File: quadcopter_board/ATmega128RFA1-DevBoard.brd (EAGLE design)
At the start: 57.1 x 53.3 mm, 44 parts, among them J1 ISP, J2 ARDUINO_UNO_R3, J3 POWER_JACKPTH_LOCK, U1 ATMEGA128RFA1, U2 LM1117, Y1 16MHz

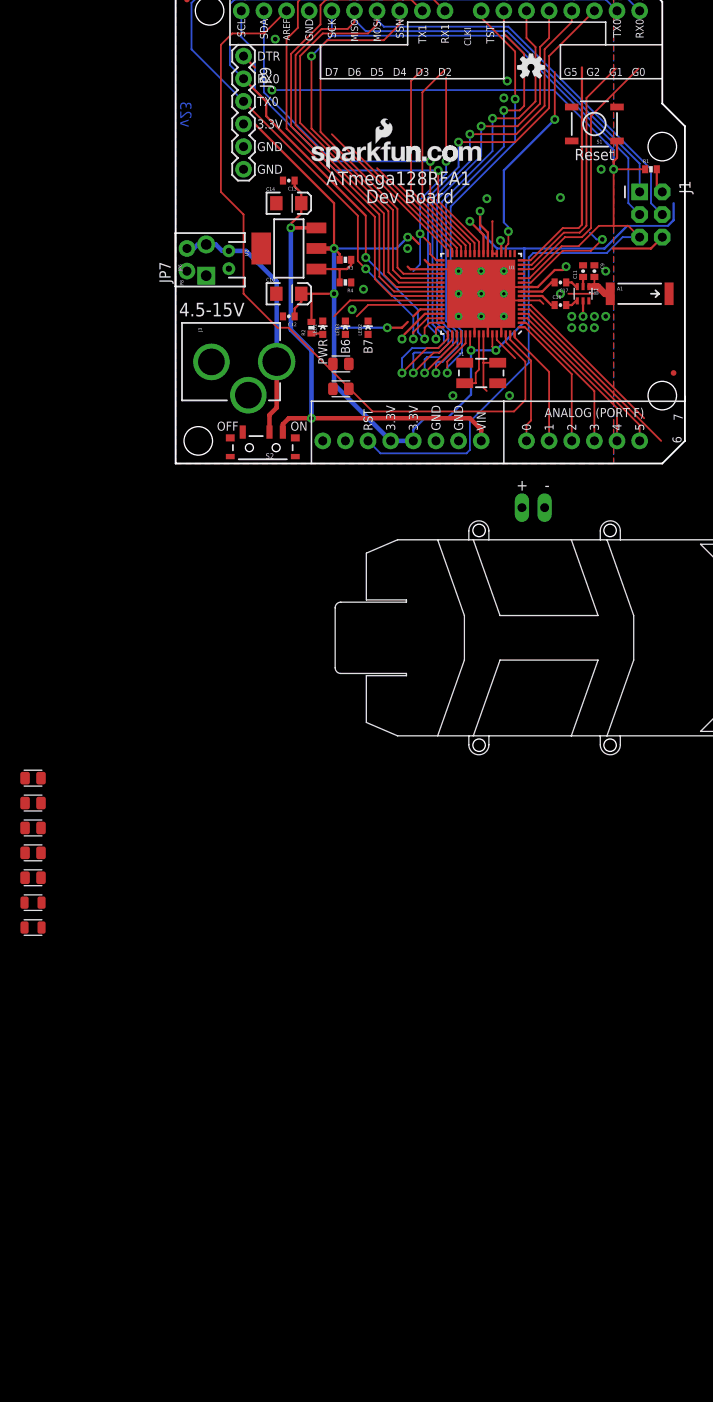
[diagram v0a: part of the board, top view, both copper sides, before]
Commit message: added and wired imu
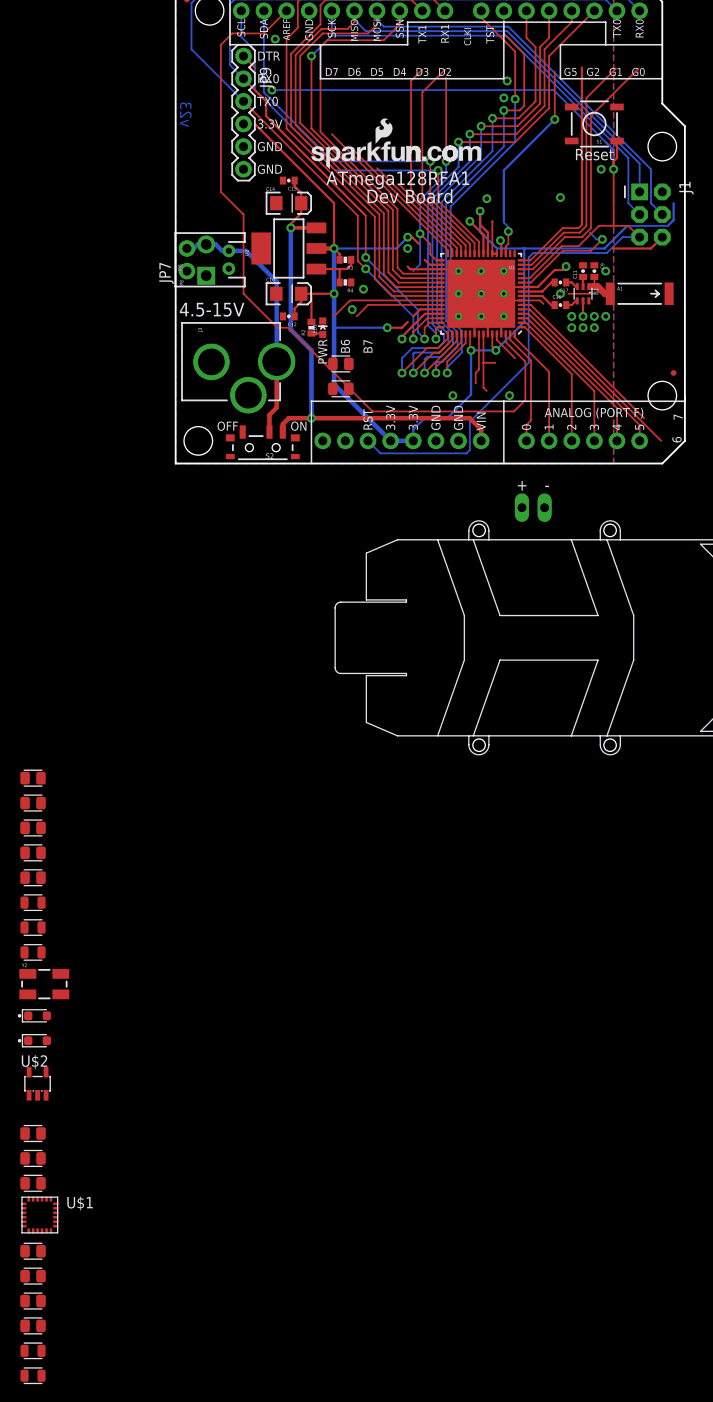
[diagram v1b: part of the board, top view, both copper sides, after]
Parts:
- removed LED2, LED3: GREEN, SparkFun-LED:LED-0603
- removed Y1: 16MHz, SparkFun-FreqCtrl:CRYSTAL-SMD-5X3
- added C1, C2: 1uF, quadparts_prebuilt:CAPC2012X140_HS
- added C18: 0.01uF, quadparts_prebuilt:CAPC2012X140_HS
- added C19: 0.1uF, quadparts_prebuilt:CAPC2012X140_HS
- added C20: 10uF, quadparts_prebuilt:CAPC2012X140_HS
- added C21: 4.7uF, quadparts_prebuilt:CAPC2012X140_HS
- added C22: 0.22uF, quadparts_prebuilt:CAPC2012X140_HS
- added D1, D2: green, quadparts_prebuilt:LEDSC125X200X120-2_HS
- added R5, R6: 10K, quadparts_prebuilt:RESC2012X60_HS
- added U$2: TPS73633-DBVT, quadparts_prebuilt:SOT23-DBV
- added Y2: (no value), quadparts_prebuilt:CRYSTAL-SMD-5X3
- R1: value 10k -> 10K; device SparkFun-Passives:0402-RES -> quadparts_prebuilt:RESC2012X60_HS
- U$1: value OSHW-LOGOS -> IMU; device SparkFun-Aesthetics:OSHW-LOGO-S -> quadparts:LGA-24_4X4MM
- moved R1 149.6 mm to (-16.0, -99.6)
- moved U$1 140.1 mm to (-15.2, -84.3)
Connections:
- new net BAT_GND: BATT1.-, C1.2, C18.2, C19.2, C2.2, C20.2, C21.1, U$1.P$2, U$1.P$22, U$1.P$23, U$1.P$3, U$1.P$4, U$1.P$5, U$1.P$6, U$2.2
- new net N$1: BATT1.+, C1.1, U$2.1, U$2.3
- new net N$12: C22.1, U$1.P$8
- new net N$14: C22.2, U$1.P$9
- new net N$15: R1.2, U$1.P$19
- new net N$16: R6.2, U$1.P$20
- new net N$5: C18.1, U$2.4
- new net N$6: C21.2, U$1.P$7
- net 3.3V: now also R5.2; no longer R1.2
- net GND: now also D1.C, D2.C; no longer LED2.C, LED3.C
- net N$13: now also D1.A; no longer LED2.A
- net N$3: now also Y2.3; no longer Y1.3
- net N$4: now also Y2.1; no longer Y1.1
- net N$8: now also D2.A; no longer LED3.A
- net RESET: now also R5.1; no longer R1.1
- net SCL: now also U$1.P$21
- net SDA: now also U$1.P$24
- net VCC: now also C19.1, C2.1, C20.1, R1.1, R6.1, U$1.P$15, U$1.P$16, U$1.P$17, U$1.P$18, U$2.5
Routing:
- net RESET: track 122.6 -> 119.1 mm
- net 3.3V: track 150.9 -> 149.0 mm
- net N$4: track 6.92 -> 5.70 mm

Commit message: added motor controller
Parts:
- removed J3: POWER_JACKPTH_LOCK, SparkFun-Connectors:POWER_JACK_PTH_LOCK
- removed JP6: (no value), SparkFun-Connectors:JST-2-PTH
- removed JP7: (no value), SparkFun-Connectors:1X02_NO_SILK
- removed JP8: (no value), SparkFun-Connectors:SCREWTERMINAL-3.5MM-2-NS
- added C23, C26, C29, C32: 1uf, Seeed-Capacitor-2016:C0402
- added C24, C27, C30, C33: 100uf, Seeed-Capacitor-2016:AVX-B
- added C25, C28, C31, C34: 1uf, Seeed-Capacitor-2016:C0603
- added D3, D4, D5, D6: 28V-5A, Seeed-Diode-2016:DO-214AA
- added J4: (no value), quadparts:MALE_HEADER_2X1_0.1IN
- added JP1: FTDI (Serial Only), SparkFun-Connectors:FTDI_BASIC
- added Q1, Q2, Q3, Q4: CJ2302, Seeed-Transistor-2016:SOT-23
- added R10, R12, R14, R16: 10K 1/10W, Seeed-Resistor-2016:R0603
- added R11, R13, R15, R9: 100R, Seeed-Resistor-2016:R0603
- added U$3: 0, quadparts:SMD_RESISTOR
- added U$4, U$5, U$6, U$7: MOTOR_PADS, Andranik-Lab4:MOTOR_PADS
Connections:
- removed net N$1: BATT1.+, C1.1, U$2.1, U$2.3
- new net N$17: BATT1.+, J4.1
- new net N$18: Q1.1, R10.2, R9.2
- new net N$19: C25.1, D3.+, Q1.3, U$4.V-
- new net N$21: Q2.1, R11.2, R12.2
- new net N$22: C28.1, D4.+, Q2.3, U$5.V-
- new net N$24: Q3.1, R13.2, R14.2
- new net N$25: C31.1, D5.+, Q3.3, U$6.V-
- new net N$27: Q4.1, R15.2, R16.2
- new net N$28: C34.1, D6.+, Q4.3, U$7.V-
- net 3.3V: now also C19.1, C2.1, C20.1, R1.1, R6.1, U$1.P$15, U$1.P$16, U$1.P$17, U$1.P$18, U$2.5
- net BAT_GND: now also C23.1, C24.-, C26.1, C27.-, C29.1, C30.-, C32.1, C33.-, Q1.2, Q2.2, Q3.2, Q4.2, R10.1, R12.1, R14.1, R16.1, U$3.P$1; no longer C1.2, C18.2, C19.2, C2.2, C20.2, C21.1, U$1.P$2, U$1.P$22, U$1.P$23, U$1.P$3, U$1.P$4, U$1.P$5, U$1.P$6, U$2.2
- net GND: now also C1.2, C18.2, C19.2, C2.2, C20.2, C21.1, JP1.GND, U$1.P$2, U$1.P$22, U$1.P$23, U$1.P$3, U$1.P$4, U$1.P$5, U$1.P$6, U$2.2, U$3.P$2; no longer J3.GND, J3.GNDBREAK, JP6.1, JP7.1, JP8.1
- net N$9: no longer J3.PWR, JP6.2, JP7.2, JP8.2
- net PB5: now also R9.1
- net PE3: now also R13.1
- net PE4: now also R15.1
- net PE5: now also R11.1
- net RX1: now also JP1.RXI
- net TX1: now also JP1.TXO
- net VCC: now also C1.1, C24.+, C25.2, C27.+, C28.2, C30.+, C31.2, C33.+, C34.2, D3.-, D4.-, D5.-, D6.-, J4.2, U$2.1, U$2.3, U$4.V+, U$5.V+, U$6.V+, U$7.V+; no longer C19.1, C2.1, C20.1, R1.1, R6.1, U$1.P$15, U$1.P$16, U$1.P$17, U$1.P$18, U$2.5
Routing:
- net N$9: track 29.2 -> 3.06 mm

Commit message: added bigger cap to power supply
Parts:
- removed C10, C14: 10uF, SparkFun-Passives:EIA3216
- removed LED1: RED, SparkFun-LED:LED-0603
- removed R2: 1k, SparkFun-Passives:0402-RES
- removed R3: 240, SparkFun:0402-RES
- removed R4: 390, SparkFun:0402-RES
- removed S2: (no value), SparkFun:SWITCH-SPST-SMD-A
- removed U2: LM1117, SparkFun:SOT223
- added C35: 220uF, quadparts_prebuilt:CAPMP7343X310_HS
- C1, C2: value 1uF -> 10uF
- moved C1 148.3 mm to (-16.0, -223.5)
- moved C2 148.3 mm to (-16.0, -226.3)
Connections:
- removed net FB: R3.1, R4.2, U2.1
- removed net N$2: LED1.A, R2.1
- removed net N$9: S2.2
- net 3.3V: no longer C10.A, R2.2, R3.2, U2.2
- net GND: no longer C10.C, C14.C, LED1.C, R4.1
- net VCC: no longer C14.A, S2.1, U2.3
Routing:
- net 3.3V: track 149.0 -> 141.1 mm
- net FB: track 6.15 -> 0.00 mm
- net VCC: track 56.5 -> 50.5 mm
- net N$9: track 3.06 -> 0.00 mm
- net N$2: track 1.31 -> 0.00 mm

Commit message: added tags
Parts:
- removed C12: 1uF, SparkFun-Passives:0402-CAP
- removed C13: 0.1uF, SparkFun-Passives:0402-CAP
- removed C35: 220uF, quadparts_prebuilt:CAPMP7343X310_HS
- removed J2: ARDUINO_UNO_R3, SparkFun-Boards:ARDUINO_UNO_R3
- removed S1: (no value), SparkFun-Electromechanical:TACTILE_SWITCH_SMD
- added C10: 0.75pF, quadparts_prebuilt:CAPC2012X140_HS
- added C14: 22pF, quadparts_prebuilt:CAPC2012X140_HS
- C16: value JUMP -> 1uF; device SparkFun:0402-CAP -> quadparts_prebuilt:CAPC2012X140_HS
- C17: value JUMP -> 0.1uF; device SparkFun:0402-CAP -> quadparts_prebuilt:CAPC2012X140_HS
- moved C17 264.5 mm to (-16.0, -237.5), turned to 0 degrees
- moved C16 259.3 mm to (-16.0, -234.7)
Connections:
- removed net N$10: B1.4, C16.2
- removed net N$11: B1.3, C17.1
- net 3.3V: now also C16.1; no longer C12.1, J2.3.3V, J2.5V
- net A0: no longer J2.A0
- net A1: no longer J2.A1
- net A2: no longer J2.A2
- net A3: no longer J2.A3
- net A4: no longer J2.A4
- net A5: no longer J2.A5
- net AREF: no longer J2.AREF
- net GND: now also C16.2, C17.2; no longer C12.2, C13.2, J2.GND@0, J2.GND@1, J2.GND@2, S1.3
- net MISO: no longer J2.D12
- net MOSI: no longer J2.D11
- net PB4: no longer J2.D9
- net PB5: no longer J2.D8
- net PE2: no longer J2.D2
- net PE3: no longer J2.D3
- net PE4: now also C32.2; no longer J2.D4
- net PE5: no longer J2.D5
- net PE6: no longer J2.D6
- net PE7: no longer J2.D7
- net RESET: no longer J2.RES, S1.1
- net RFN: now also B1.3; no longer C17.2
- net RFP: now also B1.4; no longer C16.1
- net RX0: no longer J2.RX
- net SCK: no longer J2.D13
- net SCL: no longer J2.SCL
- net SDA: no longer J2.SDA
- net SSN: no longer J2.D10
- net TX0: no longer J2.TX
- net VCC: now also C17.1; no longer C13.1, J2.VIN
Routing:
- net 3.3V: track 141.1 -> 71.2 mm, vias 7 -> 3
- net VCC: track 50.5 -> 0.00 mm, vias 2 -> 0
- net SDA: track 43.4 -> 34.3 mm
- net A1: track 13.6 -> 5.87 mm
- net A2: track 15.3 -> 7.84 mm
- net PE2: track 50.5 -> 43.3 mm
- net A3: track 17.0 -> 11.4 mm
- net RESET: track 119.1 -> 115.2 mm
- net A4: track 18.6 -> 14.9 mm
- net AREF: track 83.9 -> 80.3 mm
- net PE4: track 58.6 -> 55.5 mm
- net PE5: track 55.8 -> 52.7 mm
- net SCL: track 45.1 -> 42.1 mm
- net RX0: track 104.2 -> 101.3 mm
- net SCK: track 85.4 -> 82.6 mm
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
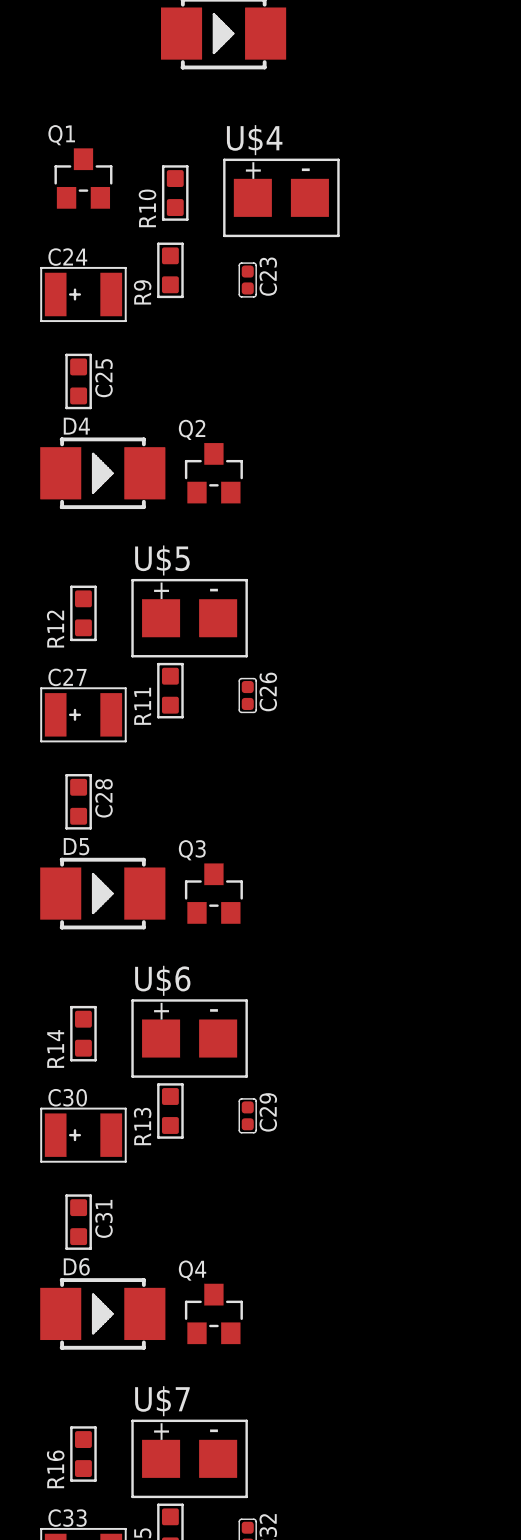
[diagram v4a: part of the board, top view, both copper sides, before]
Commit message: clear up of motor driver layout
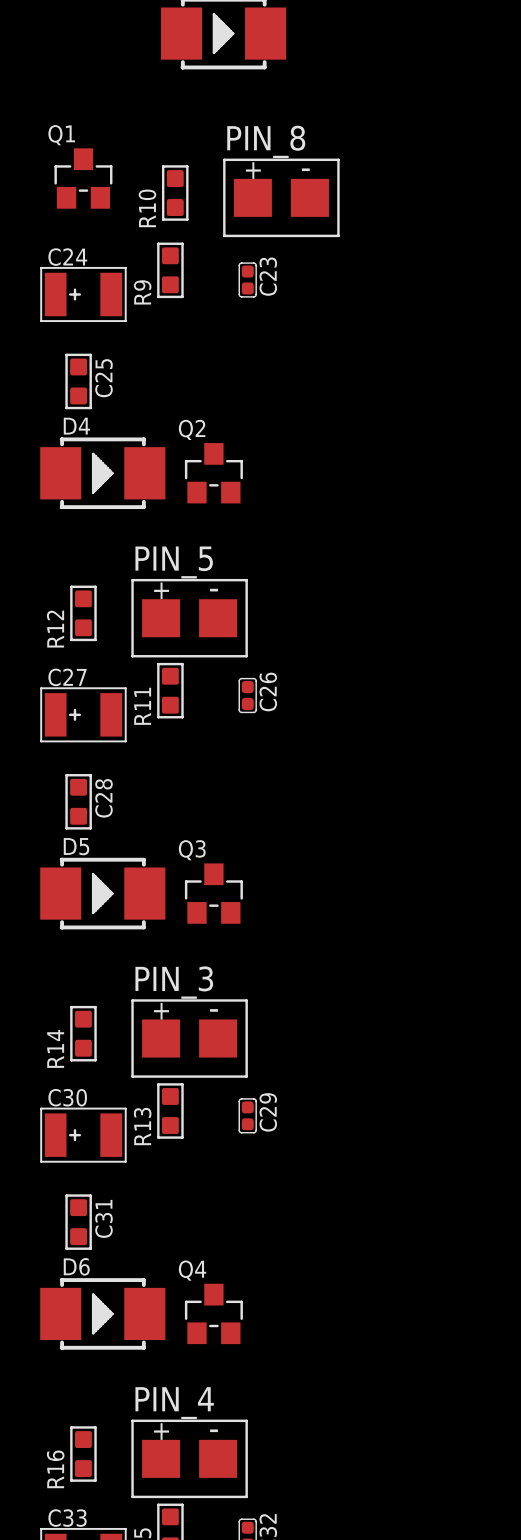
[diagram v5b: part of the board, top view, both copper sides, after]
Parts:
- renumbered U$4 to PIN_8, U$5 to PIN_5, U$6 to PIN_3, U$7 to PIN_4
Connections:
- net PB5: now also C23.2
- net PE3: now also C29.2
- net PE5: now also C26.2
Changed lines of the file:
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@@
 <attribute name="MPN" value="TAJB107M010#NJ" x="-38.1" y="-124.206" size="1.778" layer="27" display="off"/>
 </element>
-<element name="U$4" library="Andranik-Lab4" package="MOTOR_PADS" value="MOTOR_PADS" x="-5.588" y="-138.938"/>
+<element name="PIN_8" library="Andranik-Lab4" package="MOTOR_PADS" value="MOTOR_PADS" x="-5.588" y="-138.938"/>
 <element name="D3" library="Seeed-Diode-2016" package="DO-214AA" value="28V-5A" x="-8.128" y="-130.302">
 <attribute name="MPN" value="SS54B" x="-37.084" y="-136.652" size="1.778" layer="27" display="off"/>
@@
 <attribute name="MPN" value="TAJB107M010#NJ" x="-38.1" y="-147.32" size="1.778" layer="27" display="off"/>
 </element>
-<element name="U$5" library="Andranik-Lab4" package="MOTOR_PADS" value="MOTOR_PADS" x="-10.414" y="-161.036"/>
+<element name="PIN_5" library="Andranik-Lab4" package="MOTOR_PADS" value="MOTOR_PADS" x="-10.414" y="-161.036"/>
 <element name="D4" library="Seeed-Diode-2016" package="DO-214AA" value="28V-5A" x="-14.478" y="-153.416">
 <attribute name="MPN" value="SS54B" x="-37.084" y="-159.766" size="1.778" layer="27" display="off"/>
@@
 <attribute name="MPN" value="TAJB107M010#NJ" x="-38.1" y="-169.418" size="1.778" layer="27" display="off"/>
 </element>
-<element name="U$6" library="Andranik-Lab4" package="MOTOR_PADS" value="MOTOR_PADS" x="-10.414" y="-183.134"/>
+<element name="PIN_3" library="Andranik-Lab4" package="MOTOR_PADS" value="MOTOR_PADS" x="-10.414" y="-183.134"/>
 <element name="D5" library="Seeed-Diode-2016" package="DO-214AA" value="28V-5A" x="-14.478" y="-175.514">
 <attribute name="MPN" value="SS54B" x="-37.084" y="-181.864" size="1.778" layer="27" display="off"/>
@@
 <attribute name="MPN" value="TAJB107M010#NJ" x="-38.1" y="-191.516" size="1.778" layer="27" display="off"/>
 </element>
-<element name="U$7" library="Andranik-Lab4" package="MOTOR_PADS" value="MOTOR_PADS" x="-10.414" y="-205.232"/>
+<element name="PIN_4" library="Andranik-Lab4" package="MOTOR_PADS" value="MOTOR_PADS" x="-10.414" y="-205.232"/>
 <element name="D6" library="Seeed-Diode-2016" package="DO-214AA" value="28V-5A" x="-14.478" y="-197.612">
 <attribute name="MPN" value="SS54B" x="-37.084" y="-203.962" size="1.778" layer="27" display="off"/>
@@
 <wire x1="31.54" y1="13.76" x2="27.94" y2="10.16" width="0.2032" layer="1"/>
 <contactref element="R11" pad="1"/>
+<contactref element="C26" pad="2"/>
+<wire x1="-6.858" y1="-165.5445" x2="-10.922" y2="-164.084" width="0" layer="19" extent="1-1"/>
 <wire x1="27.94" y1="10.16" x2="-10.922" y2="-164.084" width="0" layer="19" extent="1-16"/>
 </signal>
@@
 <wire x1="28.194" y1="12.954" x2="25.4" y2="10.16" width="0.2032" layer="1"/>
 <contactref element="R13" pad="1"/>
+<contactref element="C29" pad="2"/>
+<wire x1="-6.858" y1="-187.6425" x2="-10.922" y2="-186.182" width="0" layer="19" extent="1-1"/>
 <wire x1="25.4" y1="10.16" x2="-10.922" y2="-186.182" width="0" layer="19" extent="1-16"/>
 </signal>
@@
 <wire x1="14.478" y1="52.578" x2="28.448" y2="52.578" width="0.2032" layer="1"/>
 <contactref element="R9" pad="1"/>
+<contactref element="C23" pad="2"/>
+<wire x1="-6.858" y1="-143.7005" x2="-10.922" y2="-141.986" width="0" layer="19" extent="1-1"/>
 <wire x1="24.253" y1="18.8" x2="-10.922" y2="-141.986" width="0" layer="19" extent="1-1"/>
 </signal>
@@
 <contactref element="J4" pad="2"/>
 <contactref element="C24" pad="+"/>
-<contactref element="U$4" pad="V+"/>
+<contactref element="PIN_8" pad="V+"/>
 <contactref element="D3" pad="-"/>
 <contactref element="C25" pad="2"/>
 <contactref element="C27" pad="+"/>
-<contactref element="U$5" pad="V+"/>
+<contactref element="PIN_5" pad="V+"/>
 <contactref element="D4" pad="-"/>
 <contactref element="C28" pad="2"/>
 <contactref element="C30" pad="+"/>
-<contactref element="U$6" pad="V+"/>
+<contactref element="PIN_3" pad="V+"/>
 <contactref element="D5" pad="-"/>
 <contactref element="C31" pad="2"/>
 <contactref element="C33" pad="+"/>
-<contactref element="U$7" pad="V+"/>
+<contactref element="PIN_4" pad="V+"/>
 <contactref element="D6" pad="-"/>
 <contactref element="C34" pad="2"/>
@@
 <signal name="N$19" class="1">
 <contactref element="D3" pad="+"/>
-<contactref element="U$4" pad="V-"/>
+<contactref element="PIN_8" pad="V-"/>
 <contactref element="Q1" pad="3"/>
 <contactref element="C25" pad="1"/>
@@
 <signal name="N$22" class="1">
 <contactref element="D4" pad="+"/>
-<contactref element="U$5" pad="V-"/>
+<contactref element="PIN_5" pad="V-"/>
 <contactref element="Q2" pad="3"/>
 <contactref element="C28" pad="1"/>
@@
 <signal name="N$25" class="1">
 <contactref element="D5" pad="+"/>
-<contactref element="U$6" pad="V-"/>
+<contactref element="PIN_3" pad="V-"/>
 <contactref element="Q3" pad="3"/>
 <contactref element="C31" pad="1"/>
@@
 <signal name="N$28" class="1">
 <contactref element="D6" pad="+"/>
-<contactref element="U$7" pad="V-"/>
+<contactref element="PIN_4" pad="V-"/>
 <contactref element="Q4" pad="3"/>
 <contactref element="C34" pad="1"/>
